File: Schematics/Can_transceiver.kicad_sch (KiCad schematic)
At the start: 1 part, among them U4 SN65HVD230DR

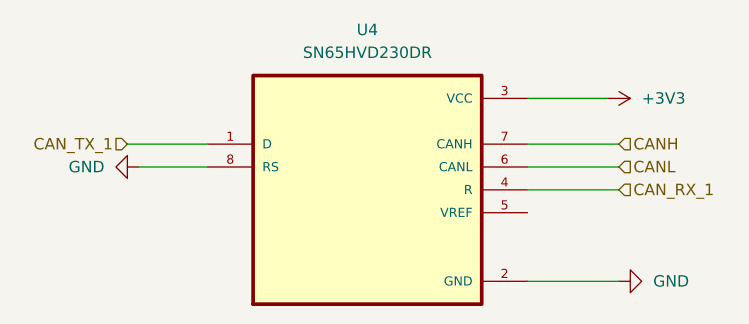
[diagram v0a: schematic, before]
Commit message: assigned footprints ready for pcb design
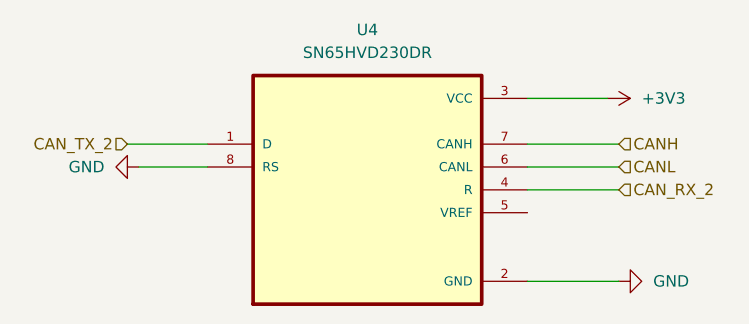
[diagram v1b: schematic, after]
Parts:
- U4: footprint SOIC127P599X175-8N -> myFootprints:SOIC127P599X175-8N
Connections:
- net CAN_RX_1 renamed CAN_RX_2
- net CAN_TX_1 renamed CAN_TX_2
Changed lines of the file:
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@@
 		)
 	)
-	(hierarchical_label "CAN_RX_1"
+	(hierarchical_label "CAN_RX_2"
 		(shape input)
 		(at 172.72 104.14 0)
@@
 		)
 	)
-	(hierarchical_label "CAN_TX_1"
+	(hierarchical_label "CAN_TX_2"
 		(shape input)
 		(at 118.11 99.06 180)
@@
 			)
 		)
-		(property "Footprint" "SOIC127P599X175-8N"
+		(property "Footprint" "myFootprints:SOIC127P599X175-8N"
 			(at 144.78 104.14 0)
 			(effects

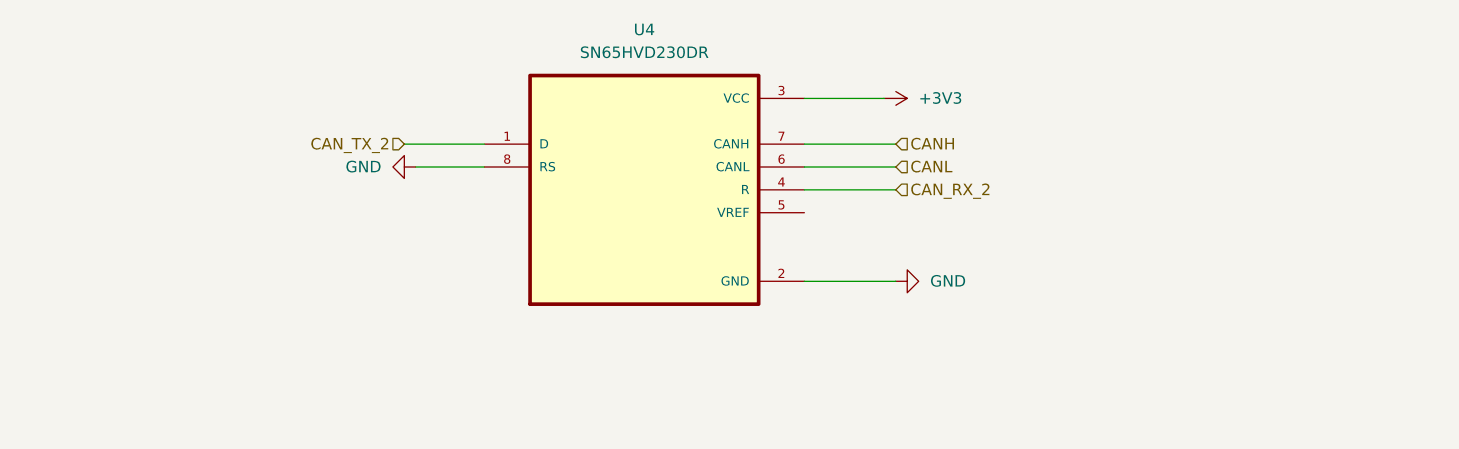
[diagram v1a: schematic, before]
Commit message: all nets are correct within PCB and correct CAN is implemented
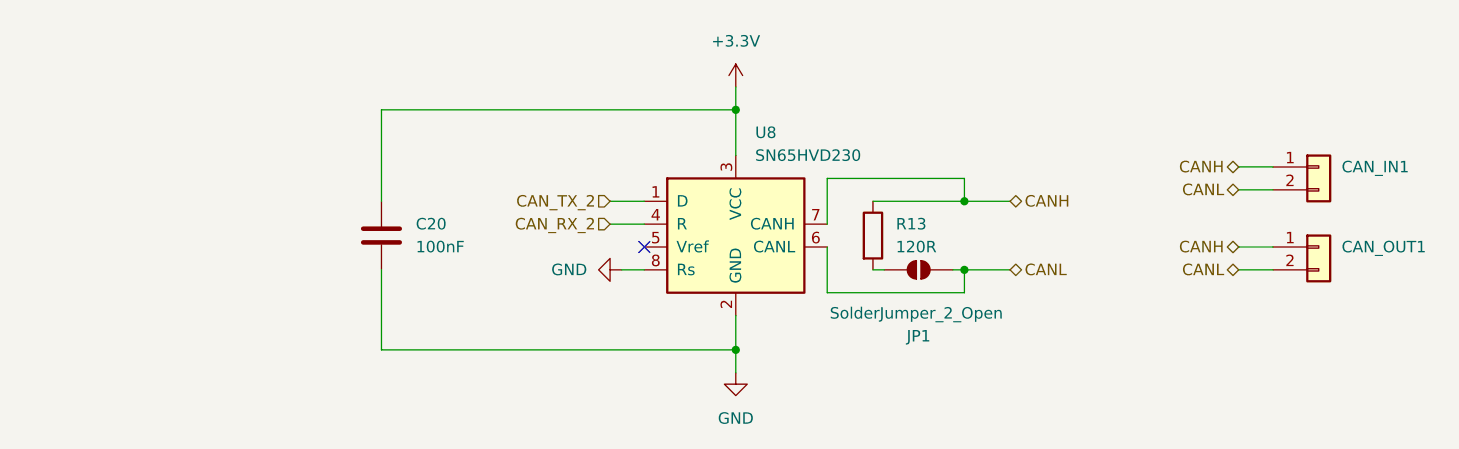
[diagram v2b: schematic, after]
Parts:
- removed U4: SN65HVD230DR, myFootprints:SOIC127P599X175-8N, symbol SN65HVD230DR:SN65HVD230DR
- added C20: 100nF, Capacitor_SMD:C_1210_3225Metric_Pad1.33x2.70mm_HandSolder, symbol Device:C
- added CAN_IN1, CAN_OUT1: ~, myFootprints:MOLEX_26013114, symbol Connector_Generic:Conn_01x02
- added JP1: SolderJumper_2_Open, Jumper:SolderJumper-2_P1.3mm_Open_TrianglePad1.0x1.5mm, symbol Jumper:SolderJumper_2_Open
- added R13: 120R, Resistor_SMD:R_0603_1608Metric, symbol Device:R
- added U8: SN65HVD230, Package_SO:SOIC-8_3.9x4.9mm_P1.27mm, symbol Interface_CAN_LIN:SN65HVD230
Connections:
- net CANH: now also CAN_IN1.1 (Pin_1), CAN_OUT1.1 (Pin_1), R13.1, U8.7 (CANH)
- net CANL: now also CAN_IN1.2 (Pin_2), CAN_OUT1.2 (Pin_2), JP1.2 (B), U8.6 (CANL)
- net CAN_RX_2: now also U8.4 (R)
- net CAN_TX_2: now also U8.1 (D)
- net GND: now also C20.2, U8.2 (GND), U8.8 (Rs)
- new net: JP1.1 (A), R13.2
- new net +3.3V: C20.1, U8.3 (VCC)
- no-connect marks 0 -> 1

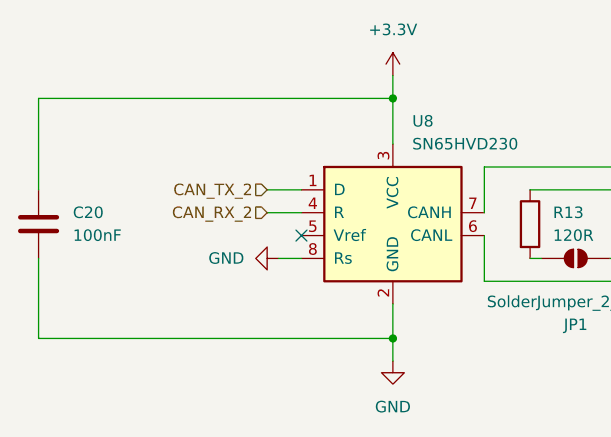
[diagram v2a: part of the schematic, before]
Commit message: routing taking place only USB to do
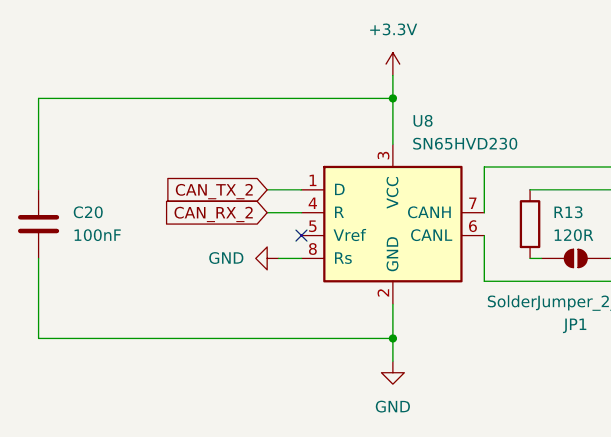
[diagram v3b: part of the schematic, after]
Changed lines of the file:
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@@
+		)
+	)
+	(global_label "CAN_TX_2"
+		(shape input)
+		(at 140.97 105.41 180)
+		(fields_autoplaced yes)
+		(effects
+			(font
+				(size 1.27 1.27)
+			)
+			(justify right)
+		)
+		(property "Intersheetrefs" "${INTERSHEET_REFS}"
+			(at 128.9739 105.41 0)
+			(effects
+				(font
+					(size 1.27 1.27)
+				)
+				(justify right)
+				(hide yes)
+			)
+		)
+	)
+	(global_label "CAN_RX_2"
+		(shape input)
+		(at 140.97 107.95 180)
+		(fields_autoplaced yes)
+		(effects
+			(font
+				(size 1.27 1.27)
+			)
+			(justify right)
+		)
+		(property "Intersheetrefs" "${INTERSHEET_REFS}"
+			(at 128.6715 107.95 0)
+			(effects
+				(font
+					(size 1.27 1.27)
+				)
+				(justify right)
+				(hide yes)
+			)
 		)
 	)
@@
 		)
 	)
-	(hierarchical_label "CAN_TX_2"
-		(shape input)
-		(at 140.97 105.41 180)
-		(effects
-			(font
-				(size 1.27 1.27)
-			)
-			(justify right)
-		)
-	)
 	(hierarchical_label "CANH"
 		(shape bidirectional)
@@
 		)
 	)
-	(hierarchical_label "CAN_RX_2"
-		(shape input)
-		(at 140.97 107.95 180)
-		(effects
-			(font
-				(size 1.27 1.27)
-			)
-			(justify right)
-		)
-	)

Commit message: Cleaned up schematic added ocilator added jtag 10 pin begining routing again
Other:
- moved on the sheet: C20, CAN_IN1, CAN_OUT1, JP1, R13, U8

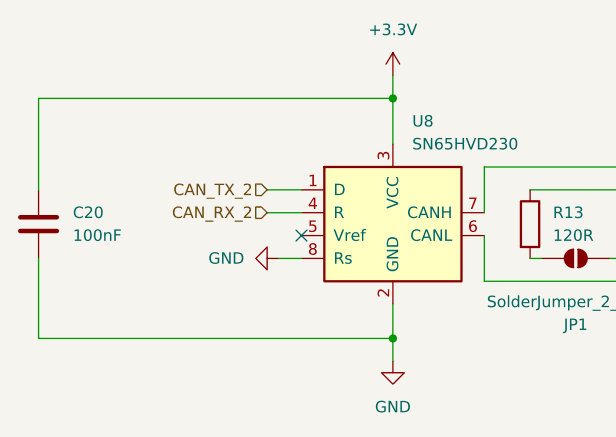
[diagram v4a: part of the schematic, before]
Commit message: second final draft finished routing added swd debug with stlink capabilities pending review for and data sheet review to ensure parts are correct, also need to edge cut ocillator
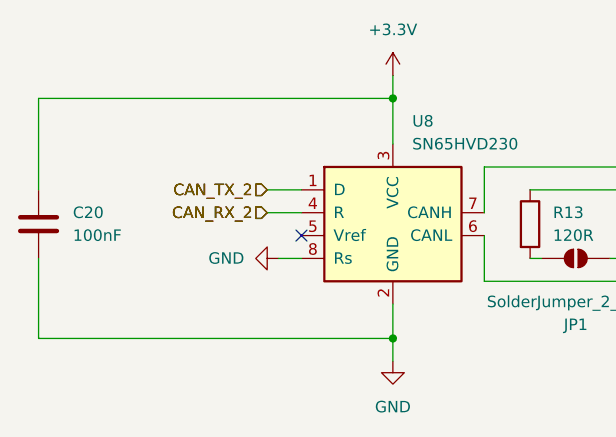
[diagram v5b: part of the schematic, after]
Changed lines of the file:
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@@
+		)
+	)
+	(hierarchical_label "CAN_TX_2"
+		(shape input)
+		(at 102.87 105.41 180)
+		(effects
+			(font
+				(size 1.27 1.27)
+			)
+			(justify right)
 		)
 	)
 	(hierarchical_label "CAN_RX_2"
 		(shape input)
+		(at 102.87 107.95 180)
+		(effects
+			(font
+				(size 1.27 1.27)
+			)
+			(justify right)
+		)
+	)
+	(hierarchical_label "CAN_RX_2"
+		(shape input)

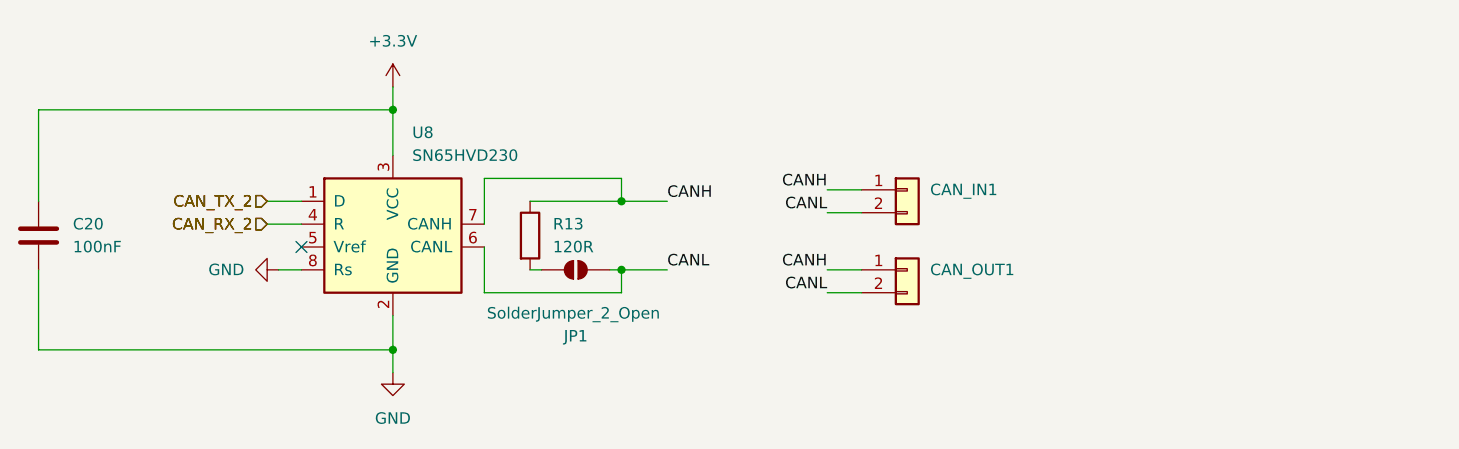
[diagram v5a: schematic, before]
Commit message: added LCSC numbers and generated BOM, fixed schematic
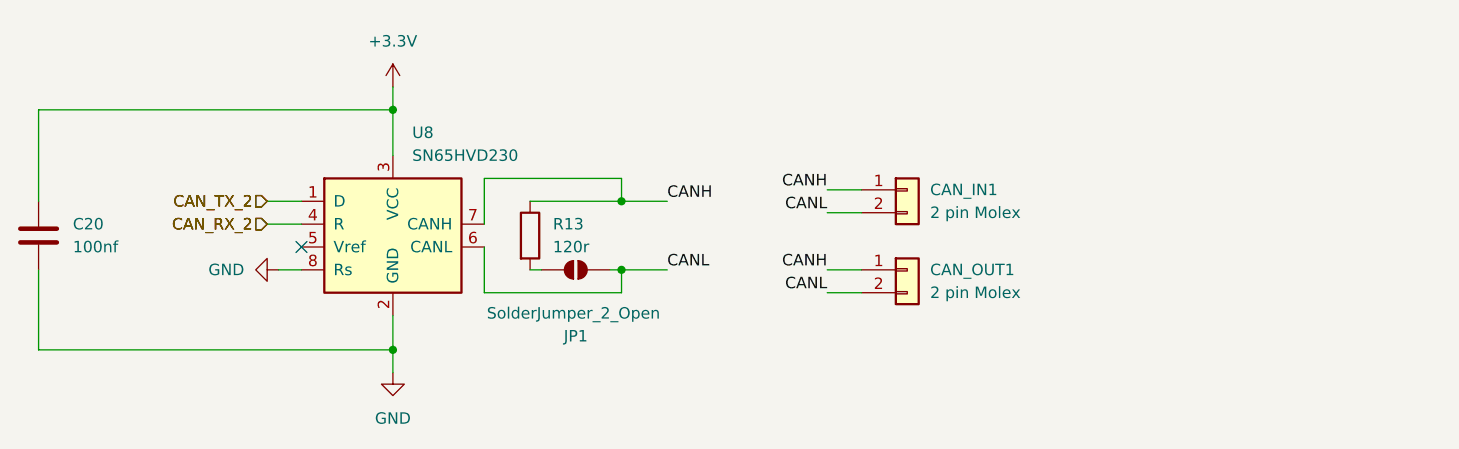
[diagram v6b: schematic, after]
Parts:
- C20: value 100nF -> 100nf; footprint Capacitor_SMD:C_1210_3225Metric_Pad1.33x2.70mm_HandSolder -> Capacitor_SMD:C_0805_2012Metric_Pad1.18x1.45mm_HandSolder; LCSC (none) -> C49393646
- CAN_IN1, CAN_OUT1: value ~ -> 2 pin Molex; LCSC (none) -> C17644051
- R13: value 120R -> 120r; LCSC (none) -> C114245
- U8: LCSC (none) -> C1543812
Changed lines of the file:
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@@
 			)
 		)
-		(property "Value" "~"
+		(property "Value" "2 pin Molex"
 			(at 176.53 106.6799 0)
 			(effects
@@
 		)
 		(property "Description" "Generic connector, single row, 01x02, script generated (kicad-library-utils/schlib/autogen/connector/)"
+			(at 173.99 104.14 0)
+			(effects
+				(font
+					(size 1.27 1.27)
+				)
+				(hide yes)
+			)
+		)
+		(property "LCSC" "C17644051"
 			(at 173.99 104.14 0)
 			(effects
@@
 			)
 		)
-		(property "Value" "100nF"
+		(property "Value" "100nf"
 			(at 81.28 110.4899 0)
 			(effects
@@
 			)
 		)
-		(property "Footprint" "Capacitor_SMD:C_1210_3225Metric_Pad1.33x2.70mm_HandSolder"
+		(property "Footprint" "Capacitor_SMD:C_0805_2012Metric_Pad1.18x1.45mm_HandSolder"
 			(at 78.4352 113.03 0)
 			(effects
@@
 		)
 		(property "lcsc" "C6565120"
+			(at 77.47 109.22 0)
+			(effects
+				(font
+					(size 1.27 1.27)
+				)
+				(hide yes)
+			)
+		)
+		(property "LCSC" "C49393646"
 			(at 77.47 109.22 0)
 			(effects
@@
 			)
 		)
+		(property "LCSC" "C1543812"
+			(at 116.84 107.95 0)
+			(effects
+				(font
+					(size 1.27 1.27)
+				)
+				(hide yes)
+			)
+		)
 		(pin "1"
 		)
@@
 			)
 		)
-		(property "Value" "120R"
+		(property "Value" "120r"
 			(at 134.62 110.4899 0)
 			(effects
@@
 		)
 		(property "lcsc" "C4353191"
+			(at 132.08 109.22 0)
+			(effects
+				(font
+					(size 1.27 1.27)
+				)
+				(hide yes)
+			)
+		)
+		(property "LCSC" "C114245"
 			(at 132.08 109.22 0)
 			(effects
@@
 			)
 		)
-		(property "Value" "~"
+		(property "Value" "2 pin Molex"
 			(at 176.53 115.5699 0)
 			(effects
@@
 			(at 173.99 113.03 0)
 			(effects
+				(font
+					(size 1.27 1.27)
+				)
+				(hide yes)
+			)
+		)
+		(property "LCSC" "C17644051"
+			(at 173.99 113.03 0)
+			(effects

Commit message: ran DRC, passed awaiting final review
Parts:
- C20: LCSC C49393646 -> C49678
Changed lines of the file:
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@@
 			)
 		)
-		(property "LCSC" "C49393646"
+		(property "LCSC" "C49678"
 			(at 77.47 109.22 0)
 			(effects

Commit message: final design pcb
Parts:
- renumbered C20 to C22, R13 to R6, U8 to U4
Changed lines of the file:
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@@
 		(on_board yes)
 		(dnp no)
-		(property "Reference" "C20"
+		(property "Reference" "C22"
 			(at 81.28 107.9499 0)
 			(effects
@@
 			(project "CameraBoard"
 				(path "/65068a32-f105-4204-b50e-234054c5a6d0/68311702-7edf-49e8-b5c7-4acffdefe23d"
-					(reference "C20")
+					(reference "C22")
 					(unit 1)
 				)
@@
 		(dnp no)
 		(fields_autoplaced yes)
-		(property "Reference" "U8"
+		(property "Reference" "U4"
 			(at 118.9833 97.79 0)
 			(effects
@@
 			(project "CameraBoard"
 				(path "/65068a32-f105-4204-b50e-234054c5a6d0/68311702-7edf-49e8-b5c7-4acffdefe23d"
-					(reference "U8")
+					(reference "U4")
 					(unit 1)
 				)
@@
 		(dnp no)
 		(fields_autoplaced yes)
-		(property "Reference" "#PWR068"
+		(property "Reference" "#PWR059"
 			(at 116.84 96.52 0)
 			(effects
@@
 			(project "CameraBoard"
 				(path "/65068a32-f105-4204-b50e-234054c5a6d0/68311702-7edf-49e8-b5c7-4acffdefe23d"
-					(reference "#PWR068")
+					(reference "#PWR059")
 					(unit 1)
 				)
@@
 		(dnp no)
 		(fields_autoplaced yes)
-		(property "Reference" "#PWR067"
+		(property "Reference" "#PWR058"
 			(at 97.79 113.03 0)
 			(effects
@@
 			(project "CameraBoard"
 				(path "/65068a32-f105-4204-b50e-234054c5a6d0/68311702-7edf-49e8-b5c7-4acffdefe23d"
-					(reference "#PWR067")
+					(reference "#PWR058")
 					(unit 1)
 				)
@@
 		(dnp no)
 		(fields_autoplaced yes)
-		(property "Reference" "R13"
+		(property "Reference" "R6"
 			(at 134.62 107.9499 0)
 			(effects
@@
 			(project "CameraBoard"
 				(path "/65068a32-f105-4204-b50e-234054c5a6d0/68311702-7edf-49e8-b5c7-4acffdefe23d"
-					(reference "R13")
+					(reference "R6")
 					(unit 1)
 				)
@@
 		(dnp no)
 		(fields_autoplaced yes)
-		(property "Reference" "#PWR069"
+		(property "Reference" "#PWR060"
 			(at 116.84 130.81 0)
 			(effects
@@
 			(project "CameraBoard"
 				(path "/65068a32-f105-4204-b50e-234054c5a6d0/68311702-7edf-49e8-b5c7-4acffdefe23d"
-					(reference "#PWR069")
-					(unit 1)
-				)
+					(reference "#PWR060")
+					(unit 1)
+				)
